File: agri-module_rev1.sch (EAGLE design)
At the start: 39 parts, among them M1 DMG1023, U2 PCA9570, U3 APDS-9960

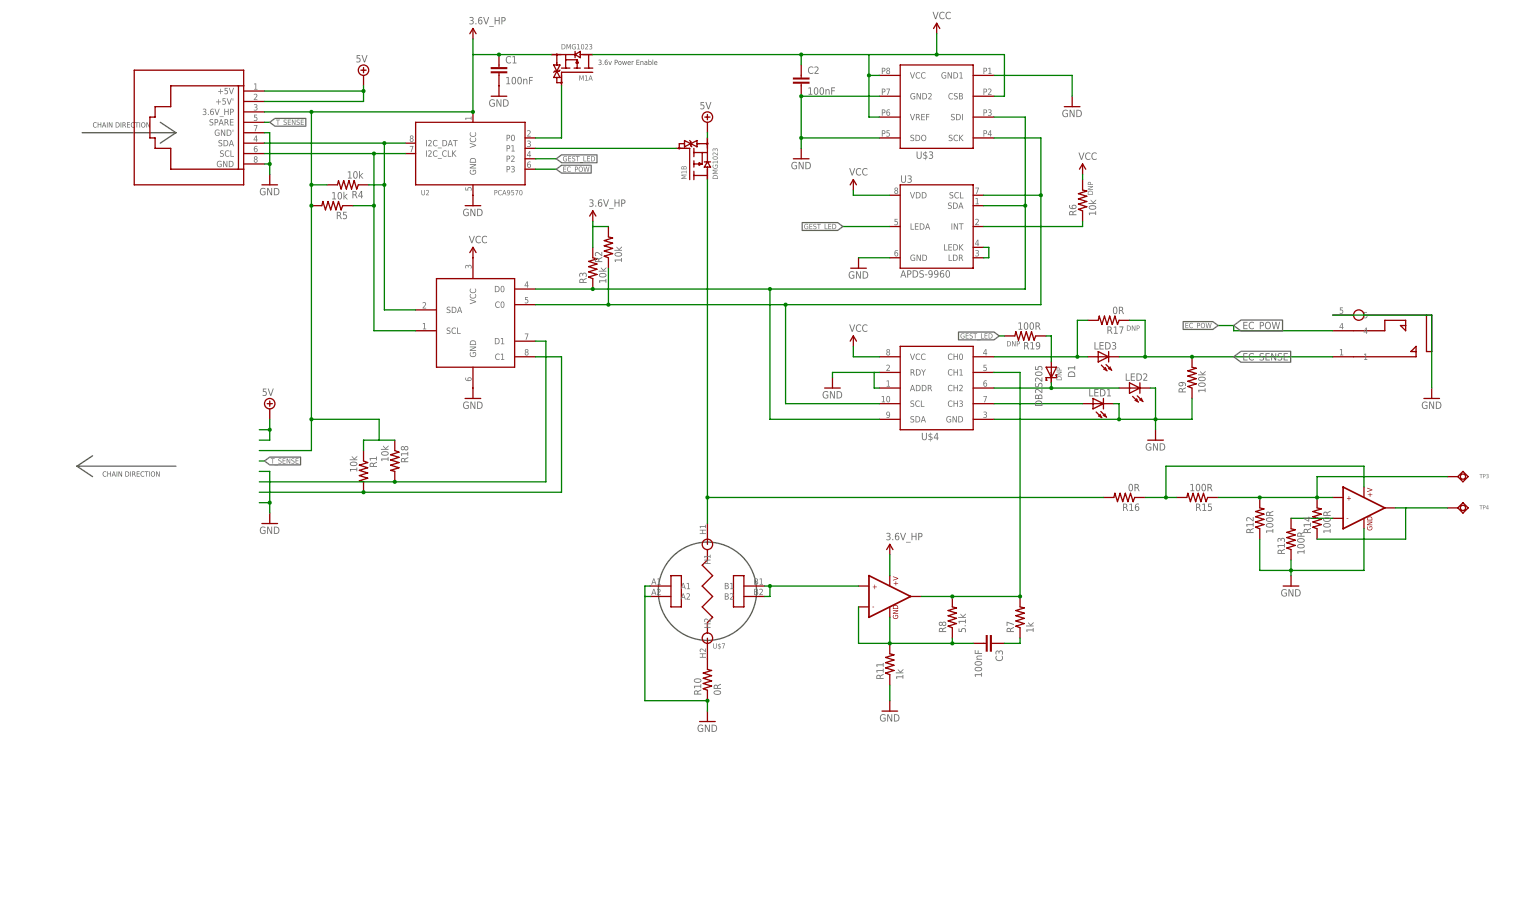
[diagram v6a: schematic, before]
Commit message: Audit 1 w/ notes (wired / ready for feedback...)
______________________________________________
Schematic Feedback:
______________________________________________|
-no "zero length" junctions to parts
-add more labels, less long/jumbled connections
-tighten up the look
-replace 5v Power FET with higher power part (6601 or SIA5)
>(These are Dual N+P fets, use as darlington. Inverts signal back
aswell...)
-add very weak pull-up/downs to any fet gates. These should never be
floating
-copy michaels de-coupl caps to apds-9960
-add atleast 0R's to everything, so you dont need to cut traces
-add "lvl-trans/isolation-filter" FETs (poor mans) to i2c lines (check
Michaels schema...)
-***change i2c switch Vcc to 3.6v_HP! (otherwise, can't talk to further
boards if off)
-add RC to any power switches, so you don't get "inrush oscillation"
-add de-coupling caps and resistors to Vcc line PER PART

______________________________________________
Layout Feedback:
______________________________________________|
-add i2c addresses to board silkscreen (helps dev)
-Add mills around parts for Thermo Isolation
-tighten width of polygone pours to match trace widths (0.2032)
-Can make vias smaller (down to 0.2!)

-Use Michael's AUX jack? Or stick with mine?

______________________________________________
Feature Changes to add/design:
______________________________________________|
-See if board can be standalone and run on 5v.
>Check if all parts can use 5v & add DIP switch.
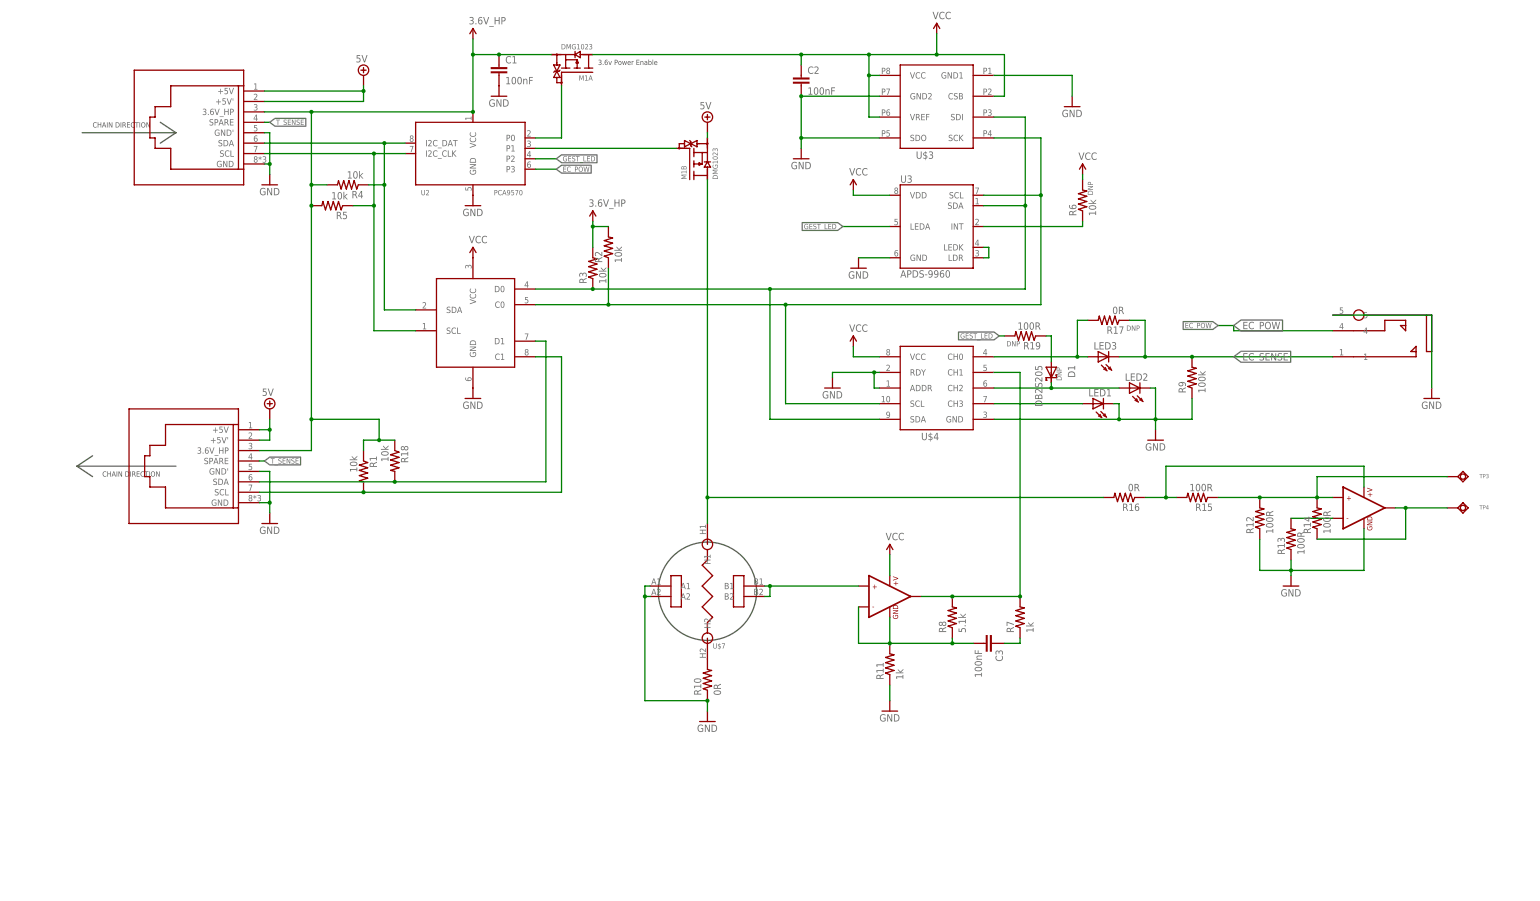
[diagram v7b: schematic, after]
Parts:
- added U$9: RJ45_RA_SMD, BrainGrid - Electromechanical:RJ45_RA_SMD
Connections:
- net 3.6V_HP: now also U$9.3.6V_HP; no longer U$5.+V
- net 5V: now also U$9.+5V, U$9.+5V'
- net GND: now also U$9.GND, U$9.GND'
- net N$7: now also U$9.SDA
- net N$8: now also U$9.SCL
- net T_SENSE: now also U$9.SPARE
- net VCC: now also U$5.+V
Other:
- note added: "Source these LEDs"
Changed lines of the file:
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@@
 <?xml version="1.0" encoding="utf-8"?>
 <!DOCTYPE eagle SYSTEM "eagle.dtd">
-<eagle version="7.5.0">
+<eagle version="7.6.0">
 <drawing>
 <settings>
@@
 <setting verticaltext="up"/>
 </settings>
-<grid distance="0.05" unitdist="inch" unit="inch" style="lines" multiple="1" display="no" altdistance="0.01" altunitdist="inch" altunit="inch"/>
+<grid distance="0.1" unitdist="inch" unit="inch" style="lines" multiple="1" display="no" altdistance="0.01" altunitdist="inch" altunit="inch"/>
 <layers>
 <layer number="1" name="Top" color="4" fill="1" visible="no" active="no"/>
@@
 <part name="SUPPLY6" library="BrainGrid - Supplies" deviceset="VCC" device=""/>
 <part name="GND10" library="BrainGrid - Supplies" deviceset="GND" device=""/>
-<part name="SUPPLY7" library="BrainGrid - Supplies" deviceset="3.6V_HP" device=""/>
 <part name="C3" library="BrainGrid - Capacitors" deviceset="C_100N" device="_0402" value="100nF"/>
 <part name="GND11" library="BrainGrid - Supplies" deviceset="GND" device=""/>
@@
 <part name="U$2" library="BrainGrid - Electromechanical" deviceset="35RASMT2BHNTRX" device=""/>
 <part name="GND14" library="BrainGrid - Supplies" deviceset="GND" device=""/>
+<part name="U$9" library="BrainGrid - Electromechanical" deviceset="RJ45_RA_SMD" device=""/>
+<part name="SUPPLY7" library="BrainGrid - Supplies" deviceset="VCC" device=""/>
 </parts>
 <sheets>
@@
 <text x="328.93" y="5.08" size="2.286" layer="90">James Hutton</text>
 <text x="326.39" y="15.24" size="1.778" layer="90">Rev 1</text>
+<text x="264.16" y="124.46" size="1.778" layer="104">Source these LEDs</text>
 </plain>
 <instances>
@@
 <instance part="SUPPLY6" gate="G$1" x="271.78" y="186.69"/>
 <instance part="GND10" gate="G$1" x="224.79" y="55.88"/>
-<instance part="SUPPLY7" gate="G$1" x="224.79" y="93.98"/>
 <instance part="C3" gate="G$1" x="248.92" y="72.39" rot="R270"/>
 <instance part="GND11" gate="G$1" x="180.34" y="53.34"/>
@@
 <instance part="U$2" gate="G$1" x="349.25" y="148.59" rot="R180"/>
 <instance part="GND14" gate="G$1" x="356.87" y="132.08"/>
+<instance part="U$9" gate="G$1" x="55.88" y="115.57"/>
+<instance part="SUPPLY7" gate="G$1" x="224.79" y="93.98"/>
 </instances>
 <busses>
@@
 <wire x1="73.66" y1="114.3" x2="73.66" y2="106.68" width="0.1524" layer="91"/>
 <junction x="73.66" y="106.68"/>
+<pinref part="U$9" gate="G$1" pin="GND'"/>
+<pinref part="U$9" gate="G$1" pin="GND"/>
 </segment>
 <segment>
@@
 <pinref part="U$4" gate="ADS1015" pin="ADDR"/>
 <pinref part="U$4" gate="ADS1015" pin="RDY"/>
+<junction x="220.98" y="138.43"/>
 </segment>
 <segment>
@@
 <pinref part="U$7" gate="G$1" pin="A1"/>
 <pinref part="U$7" gate="G$1" pin="A2"/>
+<junction x="165.1" y="83.82"/>
 </segment>
 <segment>
@@
 <wire x1="73.66" y1="121.92" x2="71.12" y2="121.92" width="0.1524" layer="91"/>
 <junction x="73.66" y="124.46"/>
+<pinref part="U$9" gate="G$1" pin="+5V"/>
+<pinref part="U$9" gate="G$1" pin="+5V'"/>
 </segment>
 <segment>
@@
 <wire x1="152.4" y1="173.99" x2="152.4" y2="175.26" width="0.1524" layer="91"/>
 <pinref part="SUPPLY2" gate="G$1" pin="3.6V_HP"/>
+<junction x="152.4" y="173.99"/>
 </segment>
 <segment>
@@
 <pinref part="C1" gate="G$1" pin="1"/>
 <junction x="129.54" y="215.9"/>
-</segment>
-<segment>
-<pinref part="SUPPLY7" gate="G$1" pin="3.6V_HP"/>
-<pinref part="U$5" gate="G$1" pin="+V"/>
-<wire x1="224.79" y1="88.9" x2="224.79" y2="93.98" width="0.1524" layer="91"/>
+<pinref part="U$9" gate="G$1" pin="3.6V_HP"/>
+<junction x="123.19" y="215.9"/>
+<junction x="100.33" y="121.92"/>
 </segment>
 </net>
@@
 <pinref part="R1" gate="G$1" pin="2"/>
 <junction x="96.52" y="109.22"/>
+<pinref part="U$9" gate="G$1" pin="SCL"/>
 </segment>
 </net>
@@
 <wire x1="104.14" y1="111.76" x2="71.12" y2="111.76" width="0.1524" layer="91"/>
 <junction x="104.14" y="111.76"/>
+<pinref part="U$9" gate="G$1" pin="SDA"/>
 </segment>
 </net>
@@
 <junction x="203.2" y="215.9"/>
 <pinref part="SUPPLY5" gate="G$1" pin="VCC"/>
+<junction x="219.71" y="215.9"/>
 </segment>
 <segment>
@@
 <pinref part="U$6" gate="G$1" pin="VCC"/>
 <pinref part="SUPPLY8" gate="G$1" pin="VCC"/>
+</segment>
+<segment>
+<pinref part="U$5" gate="G$1" pin="+V"/>
+<wire x1="224.79" y1="88.9" x2="224.79" y2="93.98" width="0.1524" layer="91"/>
+<pinref part="SUPPLY7" gate="G$1" pin="VCC"/>
 </segment>
 </net>
@@
 <wire x1="71.12" y1="116.84" x2="72.39" y2="116.84" width="0.1524" layer="91"/>
 <label x="72.39" y="116.84" size="1.27" layer="95" xref="yes"/>
+<pinref part="U$9" gate="G$1" pin="SPARE"/>
 </segment>
 </net>
@@
 <wire x1="350.52" y1="105.41" x2="360.68" y2="105.41" width="0.1524" layer="91"/>
 <pinref part="TP4" gate="TP" pin="TP"/>
+<junction x="350.52" y="105.41"/>
 </segment>
 </net>
@@
 </sheet>
 </sheets>
+<errors>
+</errors>
 </schematic>
 </drawing>

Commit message: fixed continuity errors
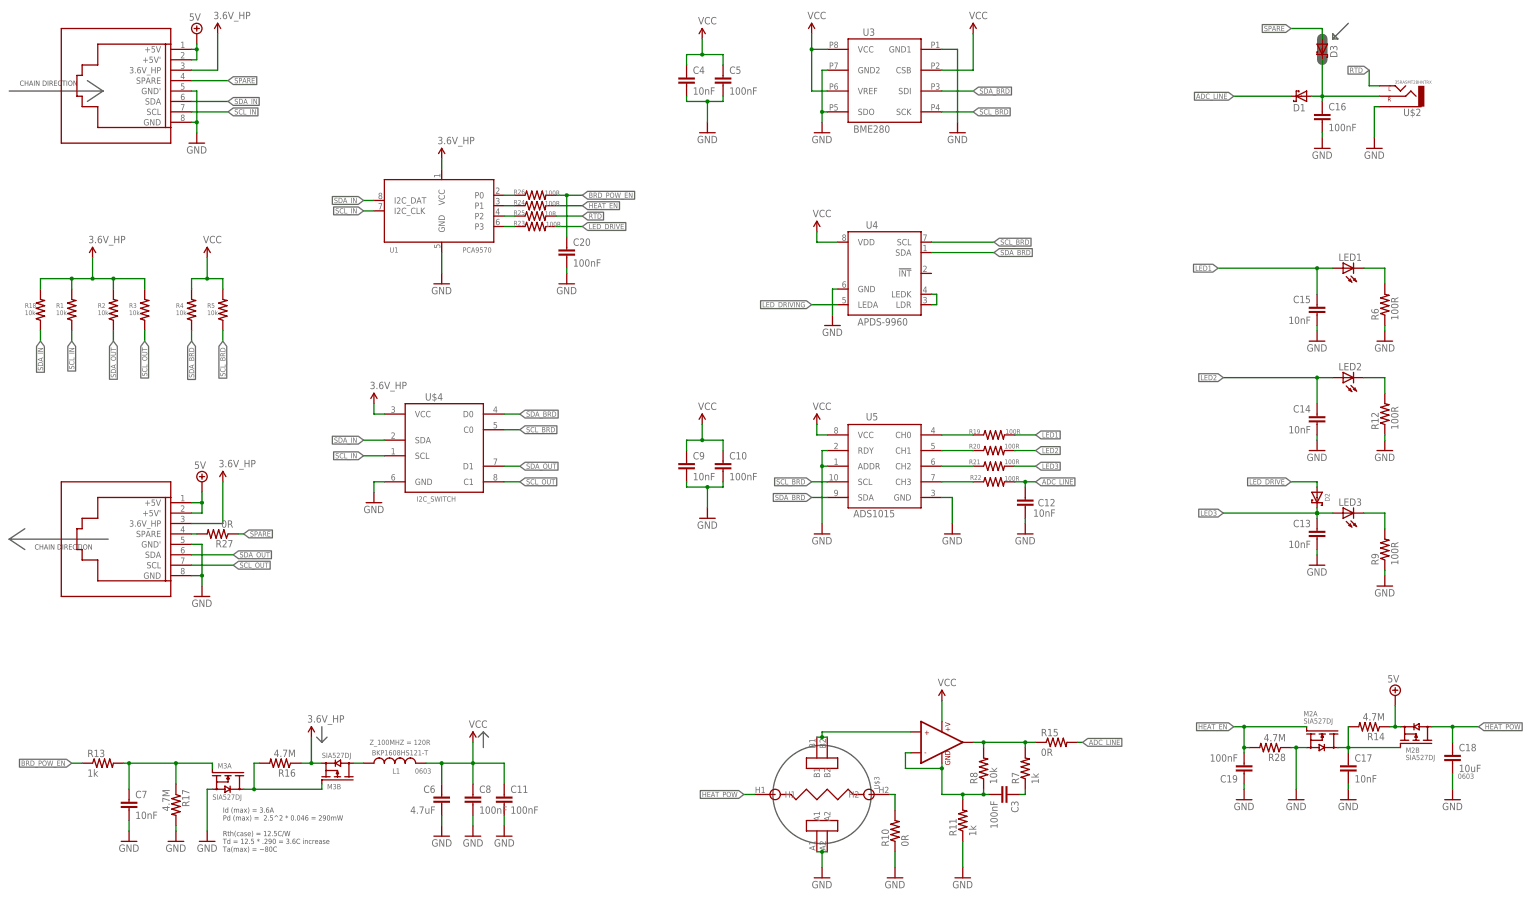
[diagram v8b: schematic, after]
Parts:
- removed C1, C2: 100nF, BrainGrid - Capacitors:C_100N_0402
- removed M1: DMG1023, BrainGrid - Transistors:DMG1023
- removed TP3, TP4: TEST_PAD, BrainGrid - Electromechanical:TEST_PAD
- removed U$6: PCA9540B_I2C_SWITCH, NXP:PCA9540B_I2C_SWITCH
- removed U$7: MG811, BrainGrid - Sensors:MG811
- removed U$8: MCP6001T, SparkFun-AnalogIC:MCP6001T
- removed U2: PCA9570, BrainGrid - MAC-PHY-Glue:PCA9570
- added C10, C11, C16, C19, C20, C5, C8: 100nF, BrainGrid - Capacitors:C_100N_0402
- added C12, C13, C14, C15, C17, C4, C7, C9: 10nF, BrainGrid - Capacitors:C_10N_0402
- added C18: 10uF, BrainGrid - Capacitors:C_10U_0603
- added C6: 4.7uF, BrainGrid - Capacitors:C_4.7U_0402
- added D2, D3: BAT54XV2, BrainGrid - Diodes:BAT54XV2
- added L1: L-0603, BrainGrid - Inductors:L-0603
- added M2, M3: SIA527DJ, BrainGrid - Transistors:SIA527DJ
- added R20, R21, R22, R23, R24, R26: 100R, BrainGrid - Resistors:R_100R_0402
- added R25: 10R, BrainGrid - Resistors:R_10R_0402
- added R27: 0R, BrainGrid - Resistors:R_0R_0402
- added R28: 4.7M, BrainGrid - Resistors:R_4.7M_0402
- added U1: PCA9570, BrainGrid - MAC-PHY-Glue:PCA9570
- added U4: APDS-9960, BrainGrid - Sensors:APDS-9960
- added U5: ADS1015, BrainGrid - Analog:ADS1015
- D1: value DB2S205 -> BAT54XV2; device EAP - Library:DB2S205 -> BrainGrid - Diodes:BAT54XV2; POPULATE DNP -> (none)
- R13: value 100R -> 1k; device BrainGrid - Resistors:R_100R_0402 -> BrainGrid - Resistors:R_1K_0402
- R14: value 100R -> 4.7M; device BrainGrid - Resistors:R_100R_0402 -> BrainGrid - Resistors:R_4.7M_0402
- R15: value 100R -> 0R; device BrainGrid - Resistors:R_100R_0402 -> BrainGrid - Resistors:R_0R_0402
- R16: value 0R -> 4.7M; device BrainGrid - Resistors:R_0R_0402 -> BrainGrid - Resistors:R_4.7M_0402
- R17: value 0R -> 4.7M; device BrainGrid - Resistors:R_0R_0402 -> BrainGrid - Resistors:R_4.7M_0402; POPULATE DNP -> (none)
- R19: POPULATE DNP -> (none)
- R6: value 10k -> 100R; device BrainGrid - Resistors:R_10K_0402 -> BrainGrid - Resistors:R_100R_0402; POPULATE DNP -> (none)
- R8: value 5.1k -> 10k; device BrainGrid - Resistors:R_5.1K_0402 -> BrainGrid - Resistors:R_10K_0402
- R9: value 100k -> 100R; device BrainGrid - Resistors:R_100K_0402 -> BrainGrid - Resistors:R_100R_0402
- U$3: value BME280 -> MG811; device BrainGrid - Sensors:BME280 -> BrainGrid - Sensors:MG811
- U$4: value ADS1015 -> I2C_SWITCH; device BrainGrid - Analog:ADS1015 -> BrainGrid - Transistors:I2C_SWITCH
- U3: value APDS-9960 -> BME280; device BrainGrid - Sensors:APDS-9960 -> BrainGrid - Sensors:BME280
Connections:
- removed net CO2_POW: M1B.D2, R16.2, U$7.H1
- removed net EC_POW: U$2.4, U2.P3
- removed net EC_SENSE: LED3.C, R17.1, R9.2, U$2.1
- removed net GEST_LED: R19.2, U2.P2, U3.LEDA
- removed net LED_INDICATE: D1.C, LED2.A, U$4.CH2
- removed net N$18: M1B.G2, U2.P1
- removed net N$20: R13.2, U$8.-IN1
- removed net N$21: R12.2, R14.2, R15.1, TP3.TP, U$8.+IN1
- removed net N$22: R14.1, TP4.TP, U$8.OUT1
- removed net N$23: R15.2, R16.1, U$8.+V
- removed net N$24: LED3.A, R17.2, U$4.CH0
- removed net N$5 (its old number): LED1.A, U$4.CH3
- removed net N$9: U$5.+IN1, U$7.B1, U$7.B2
- removed net T_SENSE: U$1.SPARE, U$9.SPARE
- new net 3.6V_HP_FILT: U$4.VCC
- new net ADC_LINE: C12.1, D1.C, R15.2, R22.2
- new net BRD_POW_EN: C20.1, R13.1, R26.2
- new net HEAT_EN: C19.2, M2A.G1, R24.2, R28.2
- new net HEAT_POW: C18.1, M2B.D2, U$3.H1
- new net HOST_POW_EN: C7.1, M3A.G1, R13.2, R17.1
- new net LED1: C15.1, LED1.A, R19.2
- new net LED2: C14.1, LED2.A, R20.2
- new net LED3: C13.1, D2.C, LED3.A, R21.2
- new net LED_DRIVE: D2.A, R23.2
- new net LED_DRIVING: U4.LEDA
- new net M$65: R21.1, U5.CH2
- new net N$12: L1.1, M3B.D2
- new net N$13: R25.1, U1.P2
- new net N$17: R10.2, U$3.H2
- new net N$26: M3A.D1, M3B.G2, R16.2
- new net N$66: R19.1, U5.CH0
- new net N$67: R20.1, U5.CH1
- new net N$69: R22.1, U5.CH3
- new net RTD: R25.2, U$2.LEFT
- new net SCL_BRD: R5.1, U$4.C0, U3.SCK, U4.SCL, U5.SCL
- new net SCL_IN: R1.1, U$1.SCL, U$4.SCL, U1.I2C_CLK
- new net SCL_OUT: R3.1, U$4.C1, U$9.SCL
- new net SDA_BRD: R4.1, U$4.D0, U3.SDI, U4.SDA, U5.SDA
- new net SDA_IN: R18.1, U$1.SDA, U$4.SDA, U1.I2C_DAT
- new net SDA_OUT: R2.1, U$4.D1, U$9.SDA
- new net SPARE: D3.A, R27.1, U$1.SPARE
- net 3.6V_HP: now also M3B.S2, R1.2, R16.1, R18.2, U1.VCC; no longer C1.1, M1A.S2, R1.1, R18.1, R4.2, R5.2, U2.VCC
- net 5V: now also M2B.S2, R14.1; no longer M1B.S2
- net GND: now also C10.2, C11.2, C12.2, C13.2, C14.2, C15.2, C16.2, C17.2, C18.2, C19.1, C20.2, C4.2, C5.2, C6.2, C7.2, C8.2, C9.2, M2A.S1, M3A.S1, R17.2, R28.1, R6.1, U$2.SLEEVE, U$3.A1, U$3.A2, U1.GND, U3.GND1, U3.GND2, U3.SDO, U4.GND, U5.ADDR, U5.GND, U5.RDY; no longer C1.2, C2.2, LED1.C, LED2.C, R13.1, U$2.5, U$3.GND1, U$3.GND2, U$3.SDO, U$4.ADDR, U$4.RDY, U$6.GND, U$7.A1, U$7.A2, U$8.GND, U2.GND, U3.GND
- net N$1: now also R26.1, U1.P0; no longer M1A.G2, U2.P0
- net N$10: now also LED2.C, R12.2; no longer R6.1, U3.INT
- net N$11: now also LED3.C, R9.2; no longer R3.1, U$3.SDI, U$4.SDA, U$6.D0, U3.SDA
- net N$14: now also C17.1, M2A.D1, M2B.G2, R14.2; no longer R4.1, U$1.SDA, U$6.SDA, U2.I2C_DAT
- net N$15: now also R23.1, U1.P3; no longer R5.1, U$1.SCL, U$6.SCL, U2.I2C_CLK
- net N$16: now also R27.2, U$9.SPARE; no longer R7.2, R8.2, U$4.CH1, U$5.OUT1
- net N$2: now also U4.LDR, U4.LEDK; no longer U3.LDR, U3.LEDK
- net N$3: now also C16.1, D1.A, D3.C, U$2.RIGHT; no longer R2.1, U$3.SCK, U$4.SCL, U$6.C0, U3.SCL
- net N$4: now also LED1.C, R6.2; no longer D1.A, R19.1
- net N$6: now also R24.1, U1.P1; no longer R10.2, U$7.H2
- net N$7: now also U$3.B1, U$3.B2, U$5.+IN1; no longer R18.2, U$6.D1, U$9.SDA
- net N$8: now also R15.1, R7.2, R8.2, U$5.OUT1; no longer R1.2, U$6.C1, U$9.SCL
- net VCC: now also C10.1, C11.1, C4.1, C5.1, C6.1, C8.1, C9.1, L1.2, R4.2, R5.2, U3.CSB, U3.VCC, U3.VREF, U4.VDD, U5.VCC; no longer C2.1, M1A.D2, R6.2, U$3.CSB, U$3.VCC, U$3.VREF, U$4.VCC, U$6.VCC, U3.VDD
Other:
- note added: "ADC MULTIPLEXOR:"
- note added: "CO2 POWER:"
- note added: "CO2 SENSOR & AMP:"
- note added: "Change polarity, or use a 0R jumper, (depending on use...)"
- note added: "ENVIRONMENT SENSOR:"
- note added: "GPIO MULTIPLEXOR:"
- note added: "I2C ADDRESS: 0x48 (7 BIT), 0b1001000 READ: 0x91 (8 BIT) !WRITE!: 0x90 (8 BIT)"
- note added: "I2C BUFFER & RAIL SWITCH:"
- note added: "I2C PULL-UPS:"
- note added: "IFF BOARD POWER ENABLED:"
- note added: "IN-COMING I2C:"
- note added: "Id (max) = 3.6A Pd (max) = 2.5^2 * 0.046 = 290mW Rth(case) = 12.5C/W Td = 12.5 * .290 = 3.6C increase Ta(max) = ~80C"
- note added: "LED SENSOR / INDICATORS:"
- note added: "LIGHT SENSOR:"
- note added: "OPTIONAL AUX JACK:"
- note added: "OUT-GOING I2C:"
- note added: "POWER CONTROL AND FILTERING:"
- note removed: "3.6v Power Enable"
- note removed: "Source these LEDs"
- note removed: "adc-Mplex"
- note removed: "hot film"
- note removed: "spectra i2c / gesture"
- moved on the sheet: C3, LED1, LED2, LED3, R1, R10, R11, R12, R13, R14, R15, R16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
